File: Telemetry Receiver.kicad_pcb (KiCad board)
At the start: 2 copper layers, 68.4 x 23.5 mm, 59 parts, among them IC1 RFX2401C, J1 SMA Connector, J2 USB_A, J3 S4B-XH-A-1, U1 LM1117-3.3, U2 USBLC6-2SC6, U3 STM32L4P5RET6, U4 NRF24L01, U5 36103205S, Y1 Crystal(16MHZ)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

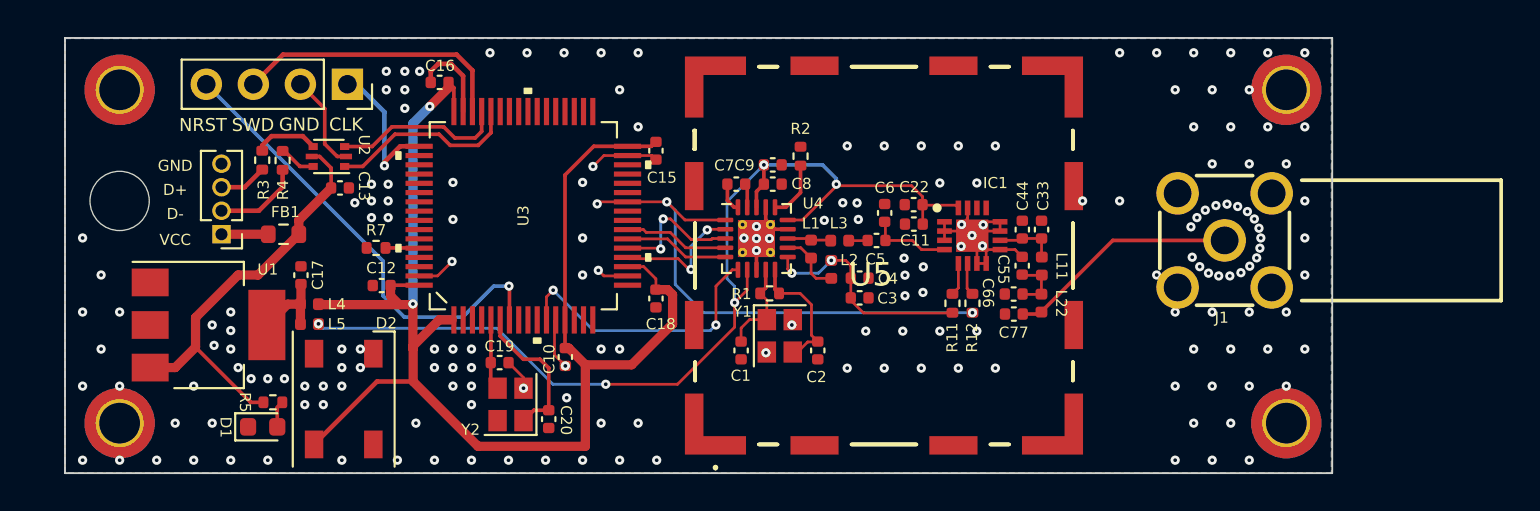
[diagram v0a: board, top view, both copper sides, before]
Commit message: Changed goldpin connector to micro usb
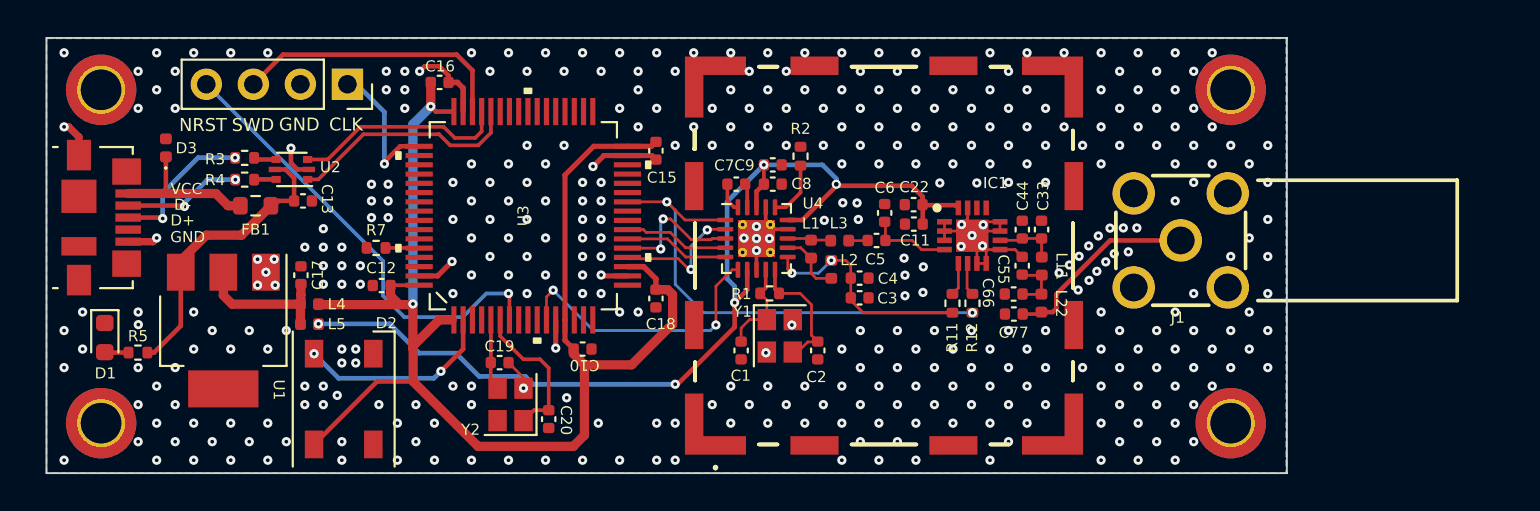
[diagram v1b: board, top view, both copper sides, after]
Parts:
- removed H5: Strain relief, MountingHole:MountingHole_3.2mm_M3_DIN965
- added D3: D_TVS, Diode_SMD:D_0402_1005Metric, F.Cu at (87.5, -92.9)
- J2: value USB_A -> USB_B_Micro; footprint Connector_PinHeader_1.27mm:PinHeader_1x04_P1.27mm_Vertical -> Connector_USB:USB_Micro-B_Molex_47346-0001
- moved D1 9.79 mm to (84.2, -82.6), turned to -90 degrees
- moved R5 7.76 mm to (86.0, -81.8), turned to 0 degrees
- moved J2 6.56 mm to (84.0, -89.1), turned to -90 degrees
- moved H1 3.00 mm to (145.0, -96.0)
- moved H4 3.00 mm to (145.0, -78.0)
- moved J1 2.37 mm to (142.3, -87.9)
- moved R4 2.30 mm to (91.8, -91.2), turned to 0 degrees
- moved FB1 2.16 mm to (92.3, -89.7)
- moved C13 2.12 mm to (94.9, -90.0)
- moved U2 2.12 mm to (94.3, -91.7)
- moved C10 1.03 mm to (110.0, -82.0), turned to 0 degrees
- moved H2 1.00 mm to (84.0, -78.0)
- moved H3 1.00 mm to (84.0, -96.0)
- moved R3 0.96 mm to (91.8, -92.3), turned to 0 degrees
- moved U1 0.85 mm to (90.6, -83.0), turned to -90 degrees
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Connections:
- D2 pad 4: unconnected-(D2-Pad4) -> /LED
- J2 pad 4: GND -> unconnected-(J2-Pad4)
- U3 pad 2: unconnected-(U3-Pad2) -> /LED
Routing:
- net /LED: track 0.00 -> 10.8 mm, vias 0 -> 2
- net VBUS: track 22.6 -> 15.9 mm
- net Net-(FB1-Pad2): track 2.53 -> 8.42 mm
- net Net-(R3-Pad1): track 2.59 -> 7.96 mm, vias 0 -> 2
- net +3.3V: track 4.45 -> 7.78 mm
- net /USB_D+: track 9.31 -> 11.6 mm
- net /USB_D-: track 10.3 -> 12.6 mm
- net Net-(R3-Pad2): track 3.48 -> 1.23 mm
- net Net-(C77-Pad1): track 12.6 -> 10.7 mm
- net Net-(R4-Pad1): track 4.76 -> 6.53 mm, vias 0 -> 2
- net NRF24_CE: track 28.6 -> 26.9 mm, vias 3 -> 2
- net GND: track 40.9 -> 39.4 mm, vias 164 -> 388
- net +3V3: track 78.4 -> 77.2 mm
- net Net-(R4-Pad2): track 2.11 -> 1.20 mm
- net /NRST: track 25.2 -> 24.6 mm
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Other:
- board size 68.4 x 23.5 mm -> 67 x 23.5 mm

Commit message: Updating the deets
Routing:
- net /RF module/3.3V_RF: track 55.8 -> 58.6 mm
- net GND: track 39.4 -> 42.0 mm, vias 388 -> 409
- net VDD_PA: track 12.3 -> 13.3 mm

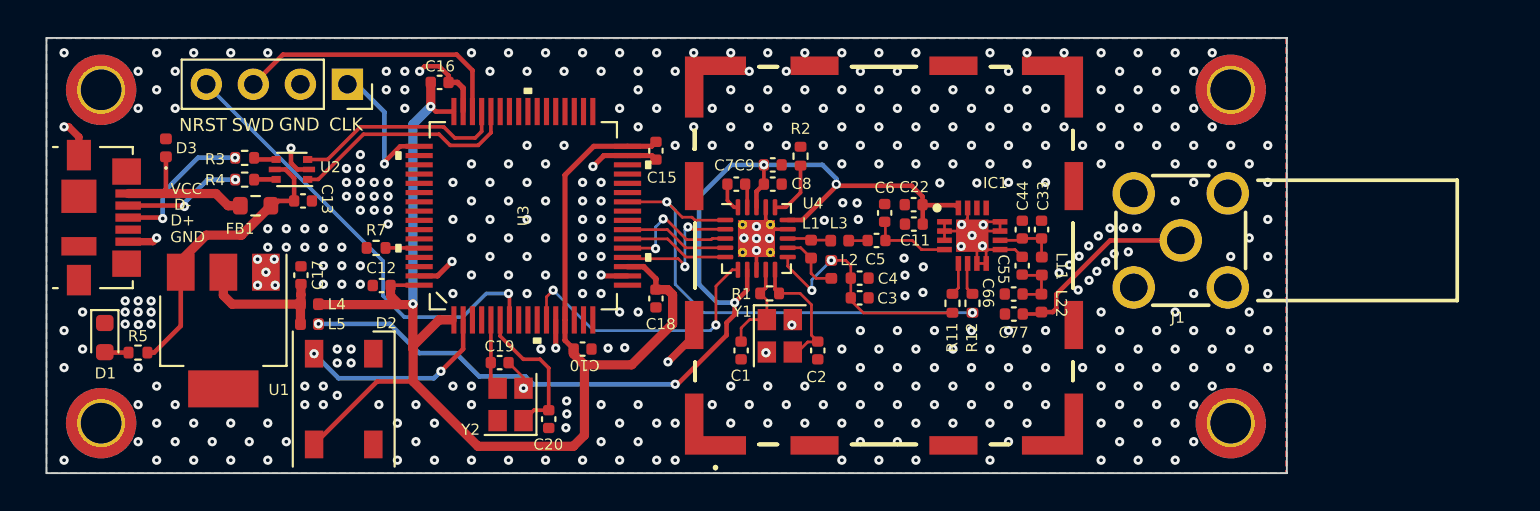
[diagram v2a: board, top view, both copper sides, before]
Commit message: 4 layer PCB
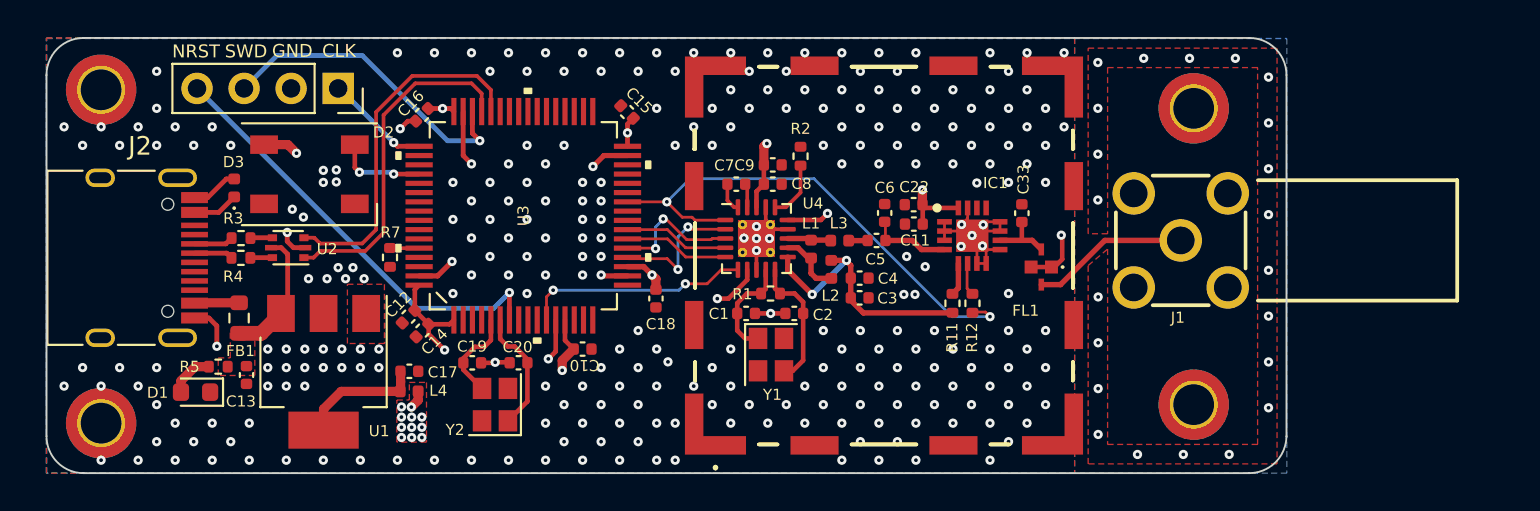
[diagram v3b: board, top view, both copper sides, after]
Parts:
- removed C44, C55, C66, C77: 1.5pF, Capacitor_SMD:C_0402_1005Metric
- removed L11, L22: 2.4nH, Inductor_SMD:L_0402_1005Metric
- removed L5: 10uH, Inductor_SMD:L_0402_1005Metric
- added C14: 100nF, Capacitor_SMD:C_0402_1005Metric, F.Cu at (101.3, -83.0)
- added FL1: 2450BP14D0100T, footprints:2450BP14D0100T, F.Cu at (134.8, -86.4)
- J2: value USB_B_Micro -> USB_C_Receptacle_USB2.0; footprint Connector_USB:USB_Micro-B_Molex_47346-0001 -> Connector_USB:USB_C_Receptacle_HRO_TYPE-C-31-M-12
- moved D2 12.3 mm to (95.2, -91.4), turned to 0 degrees
- moved C13 9.88 mm to (91.8, -80.6), turned to -90 degrees
- moved C17 7.82 mm to (100.6, -80.8), turned to 0 degrees
- moved L4 7.15 mm to (100.6, -79.7)
- moved FB1 6.13 mm to (91.5, -83.7), turned to 90 degrees
- moved U1 5.85 mm to (96.0, -80.8)
- moved D1 5.72 mm to (89.1, -79.7), turned to 180 degrees
- moved R5 4.40 mm to (90.3, -81.0)
- moved R3 4.34 mm to (91.6, -88.0)
- moved D3 4.28 mm to (91.2, -90.7)
- moved R4 4.23 mm to (91.5, -86.9)
- moved U2 4.23 mm to (94.1, -87.5)
- moved C20 3.45 mm to (106.5, -81.3), turned to 180 degrees
- moved C15 2.61 mm to (112.4, -94.8), turned to 135 degrees
- moved J2 2.39 mm to (85.0, -86.9)
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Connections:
- C11 pad 1: /RF module/3.3V_RF -> +3V3
- C22 pad 1: /RF module/3.3V_RF -> +3V3
- C8 pad 1: /RF module/3.3V_RF -> +3V3
- C9 pad 1: /RF module/3.3V_RF -> +3V3
- D3 pad 1: Net-(FB1-Pad2) -> Net-(D3-Pad1)
- FB1 pad 2: Net-(FB1-Pad2) -> Net-(D3-Pad1)
- IC1 pad 16: /RF module/3.3V_RF -> +3V3
- R3 pad 1: Net-(R3-Pad1) -> /USB_C-
- R4 pad 1: Net-(R4-Pad1) -> /USB_C+
- U2 pad 1: /USB_D- -> /USB_D+
- U2 pad 3: /USB_D+ -> /USB_D-
- U3 pad 2: /LED -> unconnected-(U3-Pad2)
- U3 pad 52: unconnected-(U3-Pad52) -> /LED
- U4 pad 15: /RF module/3.3V_RF -> +3V3
- U4 pad 18: /RF module/3.3V_RF -> +3V3
- U4 pad 7: /RF module/3.3V_RF -> +3V3
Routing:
- net /RF module/3.3V_RF: track 58.6 -> 0.00 mm, vias 5 -> 0
- net +3V3: track 77.2 -> 29.8 mm, vias 2 -> 21
- net Net-(FB1-Pad2): track 8.42 -> 0.00 mm
- net VBUS: track 15.9 -> 7.44 mm
- net Net-(R3-Pad1): track 7.96 -> 0.00 mm, vias 2 -> 0
- net /USB_D+: track 11.6 -> 18.4 mm
- net /USB_D-: track 12.6 -> 19.2 mm
- net Net-(R4-Pad1): track 6.53 -> 0.00 mm, vias 2 -> 0
- net /LED: track 10.8 -> 4.86 mm
- net Net-(D3-Pad1): track 0.00 -> 4.90 mm
- net Net-(C55-Pad1): track 3.07 -> 0.00 mm
- net /NRF24_IRQ: track 15.2 -> 12.2 mm
- net Net-(FL1-Pad2): track 10.7 -> 8.52 mm
- net /USB_C-: track 0.00 -> 2.13 mm
- net /USB_C+: track 0.00 -> 2.10 mm
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- added copper zone on F.Cu, net +3V3
- added copper zone on In2.Cu, net +3V3
- added copper zone on In1.Cu, net GND
- added copper zone on F.Cu, net VBUS
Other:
- outline, holes or cut-outs redrawn
- copper layers 2 -> 4
- board text removed: "D+"
- board text removed: "D-"
- board text removed: "VCC"

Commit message: New 3d models
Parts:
- H1, H2, H3, H4: footprint MountingHole:MountingHole_2.2mm_M2_DIN965_Pad_TopBottom -> MountingHole:MountingHole_3.2mm_M3_DIN965_Pad
- moved H2 60.7 mm to (142.5, -94.0)
- moved H1 58.7 mm to (84.3, -95.5)
- moved H3 17.5 mm to (84.3, -78.5)
- moved H4 1.12 mm to (142.5, -80.0)
- moved J1 0.87 mm to (142.3, -87.0)
- moved J2 0.50 mm to (84.5, -86.9)
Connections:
- J2 pad S1: unconnected-(J2-PadS1) -> (no net)
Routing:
- net Net-(D3-Pad1): track 4.90 -> 13.4 mm
- net +3V3: track 29.8 -> 33.3 mm
- net /USB_D+: track 18.4 -> 19.1 mm
- net GND: vias 306 -> 287
